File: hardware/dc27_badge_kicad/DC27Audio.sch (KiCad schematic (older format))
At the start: 19 parts, among them J501 SPK LEFT, J502 SPK_RIGHT, U501 CS4344-CZZ, U502 LM4880

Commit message: add gerbers for prototype
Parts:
- J501, J502: footprint Connector_PinSocket_2.54mm:PinSocket_1x02_P2.54mm_Vertical_SMD_Pin1Left -> Connector_Wire:SolderWirePad_1x02_P3.81mm_Drill0.8mm
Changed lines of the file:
@@
 F 0 "J501" H 8977 3626 50  0000 L CNN
 F 1 "SPK LEFT" H 8977 3535 50  0000 L CNN
-F 2 "Connector_PinSocket_2.54mm:PinSocket_1x02_P2.54mm_Vertical_SMD_Pin1Left" H 8950 3650 50  0001 C CNN
+F 2 "Connector_Wire:SolderWirePad_1x02_P3.81mm_Drill0.8mm" H 8950 3650 50  0001 C CNN
 F 3 "~" H 8950 3650 50  0001 C CNN
 	1    8950 3650
@@
 F 0 "J502" H 8977 4326 50  0000 L CNN
 F 1 "SPK_RIGHT" H 8977 4235 50  0000 L CNN
-F 2 "Connector_PinSocket_2.54mm:PinSocket_1x02_P2.54mm_Vertical_SMD_Pin1Left" H 8950 4350 50  0001 C CNN
+F 2 "Connector_Wire:SolderWirePad_1x02_P3.81mm_Drill0.8mm" H 8950 4350 50  0001 C CNN
 F 3 "~" H 8950 4350 50  0001 C CNN
 	1    8950 4350

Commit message: check in all datasheets, BOM tools, and start to get first fab together
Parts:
- C502: value 1mF -> 1uF
- C504, C508: footprint Capacitor_SMD:C_0603_1608Metric -> Capacitor_SMD:CP_Elec_5x5.3
- C505, C510: footprint Capacitor_SMD:C_0603_1608Metric -> MF_Passives:MF_Passives-CP6.3MM
- C509: footprint Capacitor_SMD:C_0603_1608Metric -> MF_Passives:MF_Passives-CP4MM
- R501, R502, R503, R504: footprint Resistor_SMD:R_0603_1608Metric -> Resistor_SMD:R_0805_2012Metric
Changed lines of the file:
@@
 F 0 "R503" V 5245 4100 50  0000 C CNN
 F 1 "20K" V 5336 4100 50  0000 C CNN
-F 2 "Resistor_SMD:R_0603_1608Metric" V 5490 4090 50  0001 C CNN
+F 2 "Resistor_SMD:R_0805_2012Metric" V 5490 4090 50  0001 C CNN
 F 3 "~" H 5450 4100 50  0001 C CNN
 	1    5450 4100
@@
 F 0 "R502" V 5245 3650 50  0000 C CNN
 F 1 "20K" V 5336 3650 50  0000 C CNN
-F 2 "Resistor_SMD:R_0603_1608Metric" V 5490 3640 50  0001 C CNN
+F 2 "Resistor_SMD:R_0805_2012Metric" V 5490 3640 50  0001 C CNN
 F 3 "~" H 5450 3650 50  0001 C CNN
 	1    5450 3650
@@
 F 0 "R501" V 6993 3250 50  0000 C CNN
 F 1 "20K" V 7084 3250 50  0000 C CNN
-F 2 "Resistor_SMD:R_0603_1608Metric" V 7130 3250 50  0001 C CNN
+F 2 "Resistor_SMD:R_0805_2012Metric" V 7130 3250 50  0001 C CNN
 F 3 "~" H 7200 3250 50  0001 C CNN
 	1    7200 3250
@@
 F 0 "R504" V 6943 4800 50  0000 C CNN
 F 1 "20K" V 7034 4800 50  0000 C CNN
-F 2 "Resistor_SMD:R_0603_1608Metric" V 7080 4800 50  0001 C CNN
+F 2 "Resistor_SMD:R_0805_2012Metric" V 7080 4800 50  0001 C CNN
 F 3 "~" H 7150 4800 50  0001 C CNN
 	1    7150 4800
@@
 F 0 "C504" V 5102 3650 50  0000 C CNN
 F 1 "3.3uF" V 5011 3650 50  0000 C CNN
-F 2 "Capacitor_SMD:C_0603_1608Metric" H 4850 3650 50  0001 C CNN
+F 2 "Capacitor_SMD:CP_Elec_5x5.3" H 4850 3650 50  0001 C CNN
 F 3 "~" H 4850 3650 50  0001 C CNN
 	1    4850 3650
@@
 F 0 "C508" H 2865 4396 50  0000 L CNN
 F 1 "3.3uF" H 2865 4305 50  0000 L CNN
-F 2 "Capacitor_SMD:C_0603_1608Metric" H 2750 4350 50  0001 C CNN
+F 2 "Capacitor_SMD:CP_Elec_5x5.3" H 2750 4350 50  0001 C CNN
 F 3 "~" H 2750 4350 50  0001 C CNN
 	1    2750 4350
@@
 F 0 "C509" H 4050 4400 50  0000 L CNN
 F 1 "10uF" H 4050 4300 50  0000 L CNN
-F 2 "Capacitor_SMD:C_0603_1608Metric" H 4350 4350 50  0001 C CNN
+F 2 "MF_Passives:MF_Passives-CP4MM" H 4350 4350 50  0001 C CNN
 F 3 "~" H 4350 4350 50  0001 C CNN
 	1    4350 4350
@@
 P 3500 2650
 F 0 "C502" H 3615 2696 50  0000 L CNN
-F 1 "1mF" H 3615 2605 50  0000 L CNN
+F 1 "1uF" H 3615 2605 50  0000 L CNN
 F 2 "Capacitor_SMD:C_0603_1608Metric" H 3500 2650 50  0001 C CNN
 F 3 "~" H 3500 2650 50  0001 C CNN
@@
 F 0 "C505" V 8328 3650 50  0000 C CNN
 F 1 "100uF" V 8237 3650 50  0000 C CNN
-F 2 "Capacitor_SMD:C_0603_1608Metric" H 8100 3650 50  0001 C CNN
+F 2 "MF_Passives:MF_Passives-CP6.3MM" H 8100 3650 50  0001 C CNN
 F 3 "~" H 8100 3650 50  0001 C CNN
 	1    8100 3650
@@
 F 0 "C510" V 8328 4350 50  0000 C CNN
 F 1 "100uF" V 8237 4350 50  0000 C CNN
-F 2 "Capacitor_SMD:C_0603_1608Metric" H 8100 4350 50  0001 C CNN
+F 2 "MF_Passives:MF_Passives-CP6.3MM" H 8100 4350 50  0001 C CNN
 F 3 "~" H 8100 4350 50  0001 C CNN
 	1    8100 4350

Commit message: check in all of the gerbers and artwork
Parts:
- C506: footprint Capacitor_SMD:C_0603_1608Metric -> Capacitor_SMD:CP_Elec_5x5.3
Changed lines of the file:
@@
 F 0 "C506" V 5102 4100 50  0000 C CNN
 F 1 "3.3uF" V 5011 4100 50  0000 C CNN
-F 2 "Capacitor_SMD:C_0603_1608Metric" H 4850 4100 50  0001 C CNN
+F 2 "Capacitor_SMD:CP_Elec_5x5.3" H 4850 4100 50  0001 C CNN
 F 3 "~" H 4850 4100 50  0001 C CNN
 	1    4850 4100

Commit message: temporary commit with speaker footprint and removal of fuel gauge
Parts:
- removed J501: SPK LEFT, Connector_Wire:SolderWirePad_1x02_P3.81mm_Drill0.8mm, symbol Connector:Conn_01x02_Female
- removed J502: SPK_RIGHT, Connector_Wire:SolderWirePad_1x02_P3.81mm_Drill0.8mm, symbol Connector:Conn_01x02_Female
- added LS501, LS502: Speaker, symbol Device:Speaker
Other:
- note added: "AST-01078MRR\n200mW"
- note removed: "CE20-14M-8 micro speaker x 2\n(0.25W to 0.5W max)\n"
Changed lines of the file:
@@
 Text Notes 4100 1900 0    50   ~ 10
 Audio Power Filtering\n
-$Comp
-L Connector:Conn_01x02_Female J501
-U 1 1 5C153416
-P 8950 3650
-F 0 "J501" H 8977 3626 50  0000 L CNN
-F 1 "SPK LEFT" H 8977 3535 50  0000 L CNN
-F 2 "Connector_Wire:SolderWirePad_1x02_P3.81mm_Drill0.8mm" H 8950 3650 50  0001 C CNN
-F 3 "~" H 8950 3650 50  0001 C CNN
-	1    8950 3650
-	1    0    0    -1
-$EndComp
-$Comp
-L Connector:Conn_01x02_Female J502
-U 1 1 5C15346B
-P 8950 4350
-F 0 "J502" H 8977 4326 50  0000 L CNN
-F 1 "SPK_RIGHT" H 8977 4235 50  0000 L CNN
-F 2 "Connector_Wire:SolderWirePad_1x02_P3.81mm_Drill0.8mm" H 8950 4350 50  0001 C CNN
-F 3 "~" H 8950 4350 50  0001 C CNN
-	1    8950 4350
-	1    0    0    -1
-$EndComp
 Text Notes 8850 4300 0    50   ~ 0
 +\n
@@
 Wire Wire Line
 	6350 5000 6350 5150
-Text Notes 8850 4050 0    50   ~ 0
-CE20-14M-8 micro speaker x 2\n(0.25W to 0.5W max)\n
+Text Notes 9500 3750 0    50   ~ 0
+AST-01078MRR\n200mW
 $Comp
 L Device:CP1 C504
@@
 Wire Wire Line
 	5000 3650 5300 3650
+$Comp
+L Device:Speaker LS501
+U 1 1 5CAC1626
+P 8950 3650
+F 0 "LS501" H 9120 3646 50  0000 L CNN
+F 1 "Speaker" H 9120 3555 50  0000 L CNN
+F 2 "" H 8950 3450 50  0001 C CNN
+F 3 "~" H 8940 3600 50  0001 C CNN
+	1    8950 3650
+	1    0    0    -1
+$EndComp
+$Comp
+L Device:Speaker LS502
+U 1 1 5CAC167D
+P 8950 4350
+F 0 "LS502" H 9120 4346 50  0000 L CNN
+F 1 "Speaker" H 9120 4255 50  0000 L CNN
+F 2 "" H 8950 4150 50  0001 C CNN
+F 3 "~" H 8940 4300 50  0001 C CNN
+	1    8950 4350
+	1    0    0    -1
+$EndComp
+Text Notes 9500 4450 0    50   ~ 0
+AST-01078MRR\n200mW
 $EndSCHEMATC

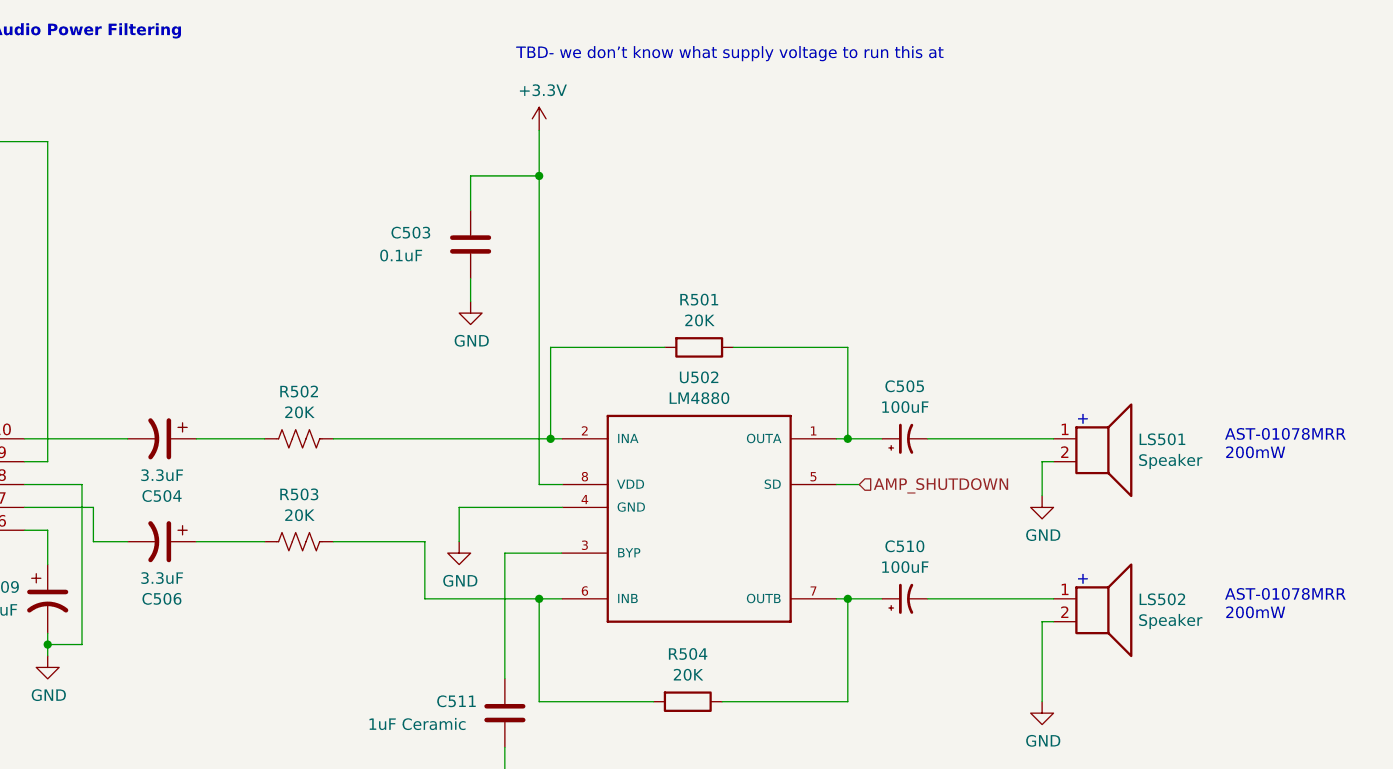
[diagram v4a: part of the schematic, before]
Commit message: add AST-01078 3d model and kicad footprint, check in current budget, update charging circut to MCP73833 instead of MCP73831:
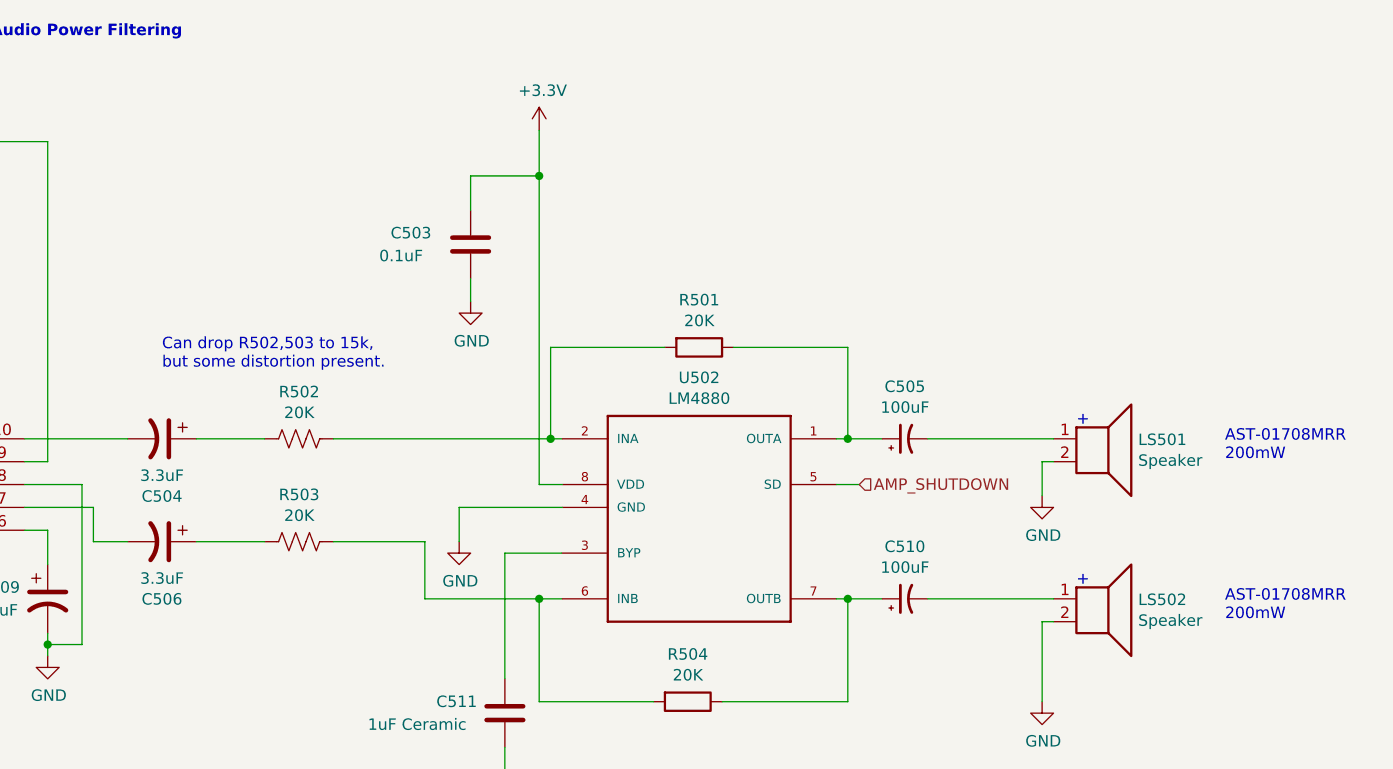
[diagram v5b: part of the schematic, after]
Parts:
- LS501, LS502: footprint (none) -> lib_fp:AST-01708-MRR
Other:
- note added: "AST-01708MRR\n200mW"
- note added: "Can drop R502,503 to 15k, \nbut some distortion present."
- note removed: "AST-01078MRR\n200mW"
- note removed: "TBD- we don’t know what supply voltage to run this at\n"
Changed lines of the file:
@@
 EESchema Schematic File Version 4
 LIBS:DC27-badge-cache
-EELAYER 26 0
+EELAYER 29 0
 EELAYER END
 $Descr A4 11693 8268
@@
 	6350 5000 6350 5150
 Text Notes 9500 3750 0    50   ~ 0
-AST-01078MRR\n200mW
+AST-01708MRR\n200mW
 $Comp
 L Device:CP1 C504
@@
 	1    0    0    -1
 $EndComp
-Text Notes 6400 2000 0    50   ~ 0
-TBD- we don’t know what supply voltage to run this at\n
 Wire Wire Line
 	6500 2300 6500 2500
@@
 F 0 "LS501" H 9120 3646 50  0000 L CNN
 F 1 "Speaker" H 9120 3555 50  0000 L CNN
-F 2 "" H 8950 3450 50  0001 C CNN
+F 2 "lib_fp:AST-01708-MRR" H 8950 3450 50  0001 C CNN
 F 3 "~" H 8940 3600 50  0001 C CNN
 	1    8950 3650
@@
 F 0 "LS502" H 9120 4346 50  0000 L CNN
 F 1 "Speaker" H 9120 4255 50  0000 L CNN
-F 2 "" H 8950 4150 50  0001 C CNN
+F 2 "lib_fp:AST-01708-MRR" H 8950 4150 50  0001 C CNN
 F 3 "~" H 8940 4300 50  0001 C CNN
 	1    8950 4350
@@
 $EndComp
 Text Notes 9500 4450 0    50   ~ 0
-AST-01078MRR\n200mW
+AST-01708MRR\n200mW
+Text Notes 4850 3350 0    50   ~ 0
+Can drop R502,503 to 15k, \nbut some distortion present.
 $EndSCHEMATC

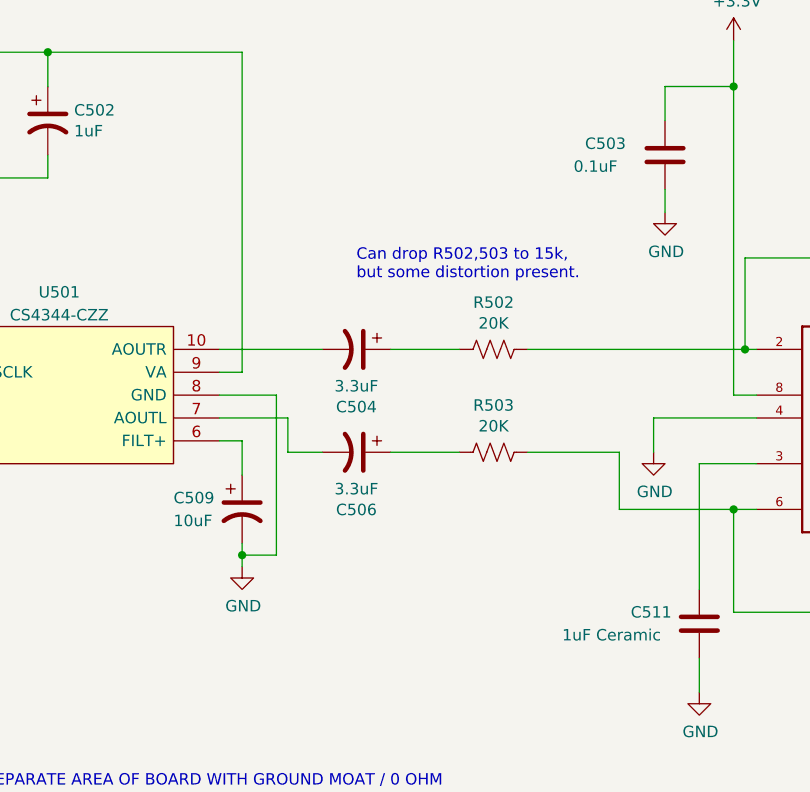
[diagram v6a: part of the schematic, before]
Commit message: add test points for the DAC. Add new context secret codes
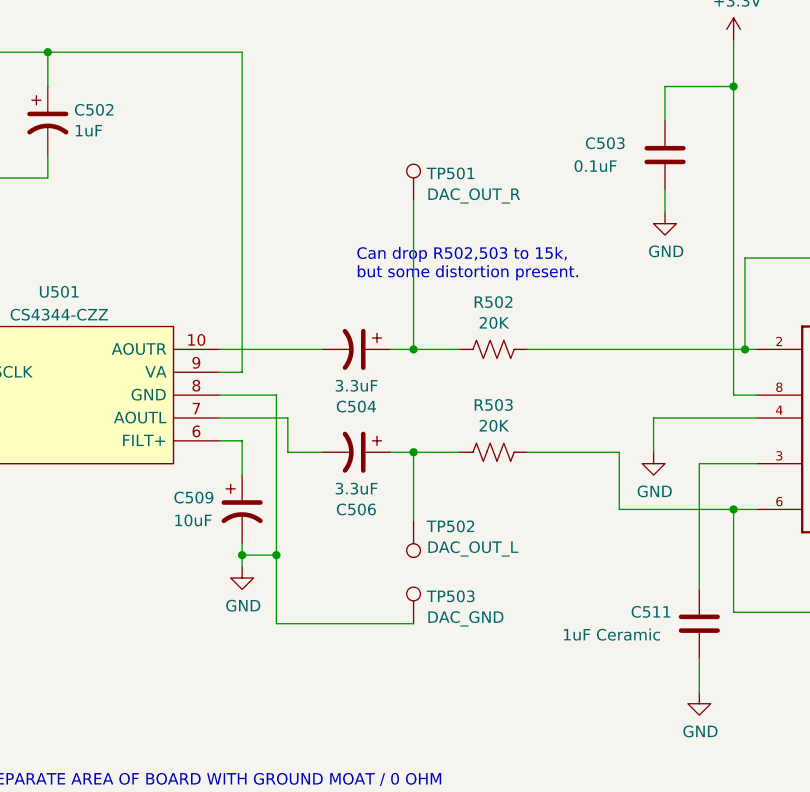
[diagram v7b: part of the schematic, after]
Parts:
- added TP501: DAC_OUT_R, TestPoint:TestPoint_Pad_D2.0mm, symbol Connector:TestPoint
- added TP502: DAC_OUT_L, TestPoint:TestPoint_Pad_D2.0mm, symbol Connector:TestPoint
- added TP503: DAC_GND, TestPoint:TestPoint_Pad_D2.0mm, symbol Connector:TestPoint
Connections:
- net GND: now also TP503.1
- net at C506.1, R503.2: now also TP502.1
- net at C504.1, R502.2: now also TP501.1
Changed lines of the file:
@@
 	2700 2350 3000 2350
 Wire Wire Line
-	5000 4100 5300 4100
+	5000 4100 5100 4100
 Wire Wire Line
 	4250 3650 4700 3650
 Wire Wire Line
-	5000 3650 5300 3650
+	5000 3650 5100 3650
 $Comp
 L Device:Speaker LS501
@@
 Text Notes 4850 3350 0    50   ~ 0
 Can drop R502,503 to 15k, \nbut some distortion present.
+$Comp
+L Connector:TestPoint TP501
+U 1 1 5CEFC925
+P 5100 3000
+F 0 "TP501" H 5158 3118 50  0000 L CNN
+F 1 "DAC_OUT_R" H 5158 3027 50  0000 L CNN
+F 2 "TestPoint:TestPoint_Pad_D2.0mm" H 5300 3000 50  0001 C CNN
+F 3 "~" H 5300 3000 50  0001 C CNN
+	1    5100 3000
+	1    0    0    -1
+$EndComp
+$Comp
+L Connector:TestPoint TP502
+U 1 1 5CEFE6CB
+P 5100 4400
+F 0 "TP502" H 5042 4426 50  0000 R CNN
+F 1 "DAC_OUT_L" H 5042 4517 50  0000 R CNN
+F 2 "TestPoint:TestPoint_Pad_D2.0mm" H 5300 4400 50  0001 C CNN
+F 3 "~" H 5300 4400 50  0001 C CNN
+	1    5100 4400
+	-1   0    0    1
+$EndComp
+Wire Wire Line
+	5100 4400 5100 4100
+Connection ~ 5100 4100
+Wire Wire Line
+	5100 4100 5300 4100
+Wire Wire Line
+	5100 3000 5100 3650
+Connection ~ 5100 3650
+Wire Wire Line
+	5100 3650 5300 3650
+$Comp
+L Connector:TestPoint TP503
+U 1 1 5CF0281F
+P 5100 4850
+F 0 "TP503" H 5158 4968 50  0000 L CNN
+F 1 "DAC_GND" H 5158 4877 50  0000 L CNN
+F 2 "TestPoint:TestPoint_Pad_D2.0mm" H 5300 4850 50  0001 C CNN
+F 3 "~" H 5300 4850 50  0001 C CNN
+	1    5100 4850
+	1    0    0    -1
+$EndComp
+Wire Wire Line
+	5100 4850 4500 4850
+Wire Wire Line
+	4500 4850 4500 4550
+Connection ~ 4500 4550
 $EndSCHEMATC
